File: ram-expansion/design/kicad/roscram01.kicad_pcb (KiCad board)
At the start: 2 copper layers, 132 x 104 mm, 29 parts, among them IC1 ATF16V8VQL-15PU, J1 Conn_02x32_Odd_Even, Q1 2N3904, U1 AS6C4008-55PCN, U2 AS6C4008-55PCN, U3 AS6C4008-55PCN, U4 AS6C4008-55PCN, U5 AS6C4008-55PCN, U6 AS6C4008-55PCN, U7 AS6C4008-55PCN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

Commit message: First cut for manufacturing
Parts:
- added REF**: roscram-jumper-config, rosco_m68k:roscram-jumper-config, B.Cu at (103.6, 50.8)
- added REF**: OSHW-Logo2_9.8x8mm_SilkScreen, Symbol:OSHW-Logo2_9.8x8mm_SilkScreen, B.Cu at (206.2, 129.3)
- added REF**: KiCad-Logo2_6mm_SilkScreen, Symbol:KiCad-Logo2_6mm_SilkScreen, B.Cu at (204.7, 43.2)
- moved JP1-3 3.88 mm to (89.0, 52.3)
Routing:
- net JP3: track 144.6 -> 148.7 mm
- net JP1: track 147.5 -> 151.5 mm
- net JP2: track 145.3 -> 148.7 mm

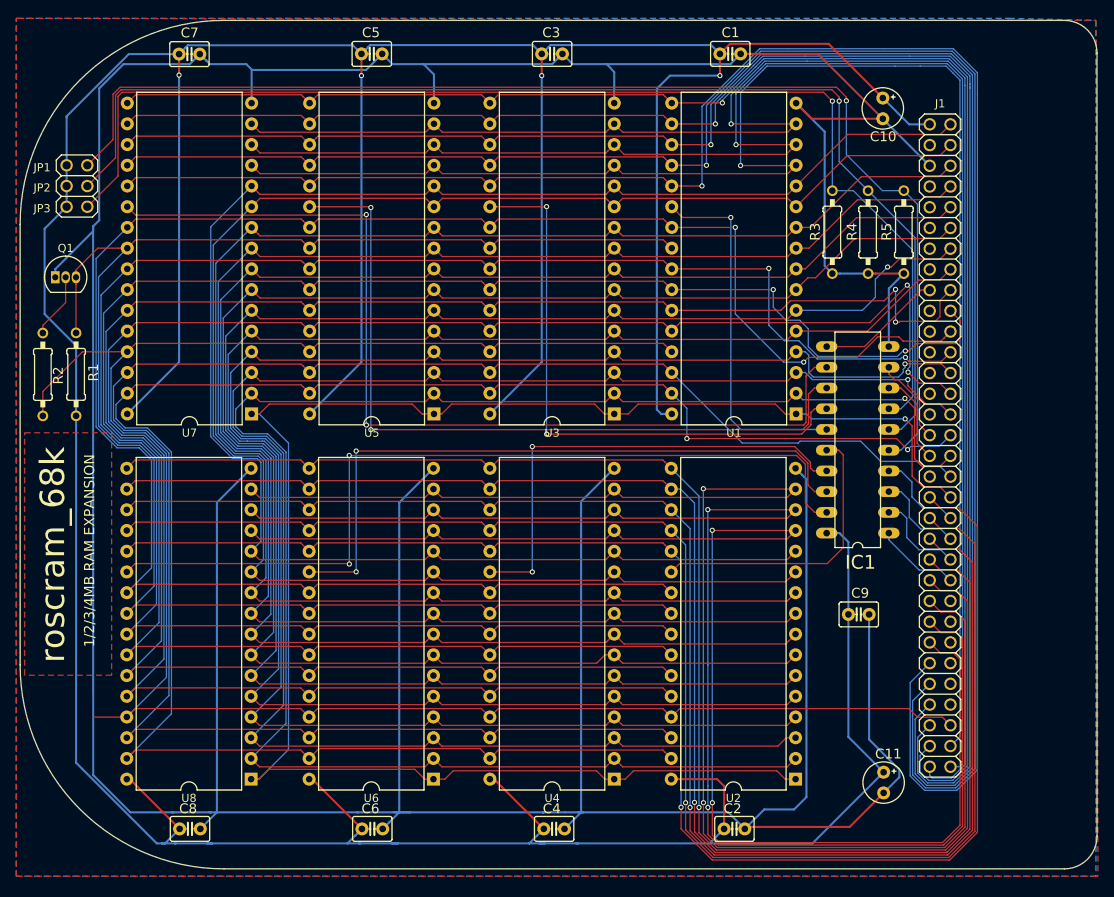
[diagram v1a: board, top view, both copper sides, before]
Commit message: Fix incorrect size and clean up
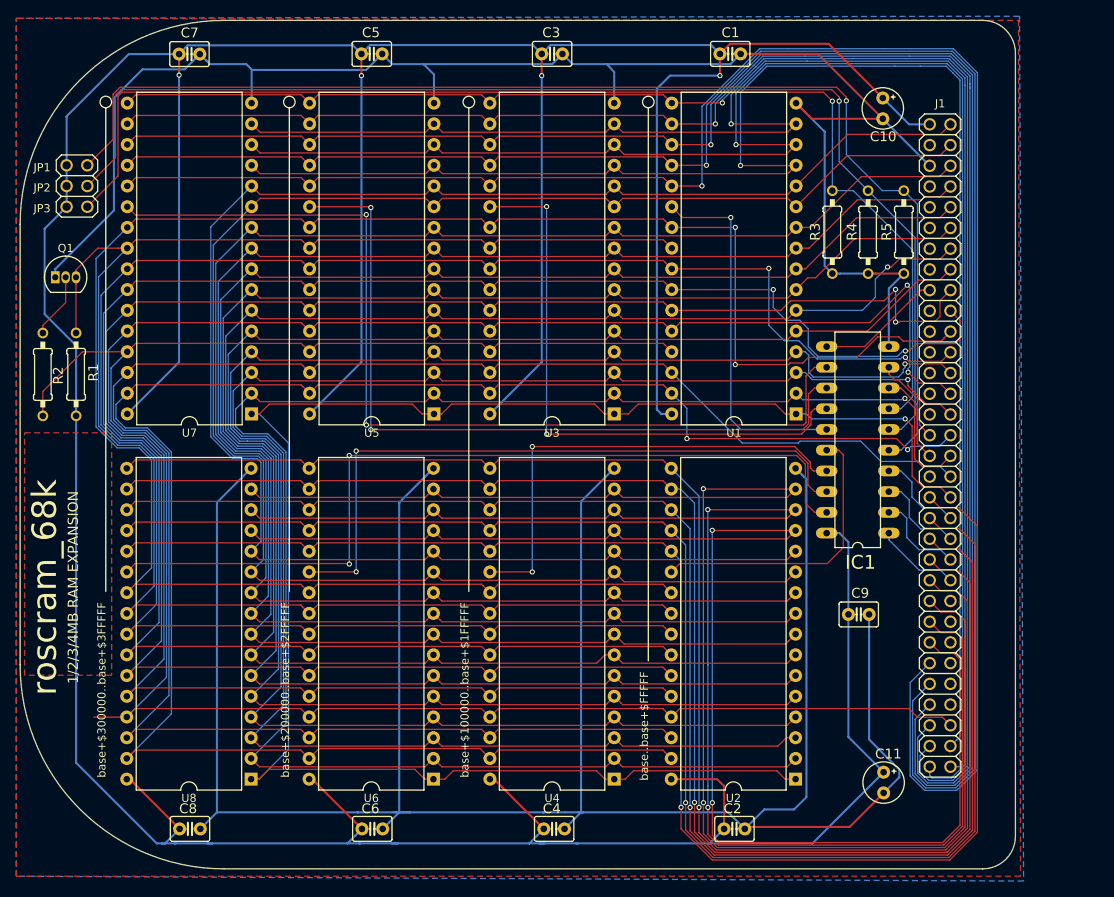
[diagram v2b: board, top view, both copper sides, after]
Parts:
- removed the REF** at (204.7, 43.2)
- moved REF** 58.4 mm to (169.4, 84.0)
- moved REF** 54.1 mm to (145.5, 85.0), turned to 180 degrees
- moved REF** 13.9 mm to (105.0, 84.0)
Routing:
- net GND: track 591.8 -> 505.3 mm
- net A11: track 239.8 -> 243.7 mm
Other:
- board size 132 x 104 mm -> 122 x 104 mm
- board text added: "Copyright ©2020 Ross Bamford & Contributors"
- board text added: "Revision 1 (May 2020)"
- board text added: "base+$100000..base+$1FFFFF"
- board text added: "base+$200000..base+$2FFFFF"
- board text added: "base+$300000..base+$3FFFFF"
- board text added: "base..base+$FFFFF"
- board text added: "https://rosco-m68k.com"
